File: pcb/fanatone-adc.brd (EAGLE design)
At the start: 49 x 32 mm, 43 parts, among them IC2 DIT4192-H, IC3 PCM4201-TSSOP-16, Q1 SST5484, U1 OPA1612AID, U2 TPS62240DRVTG4

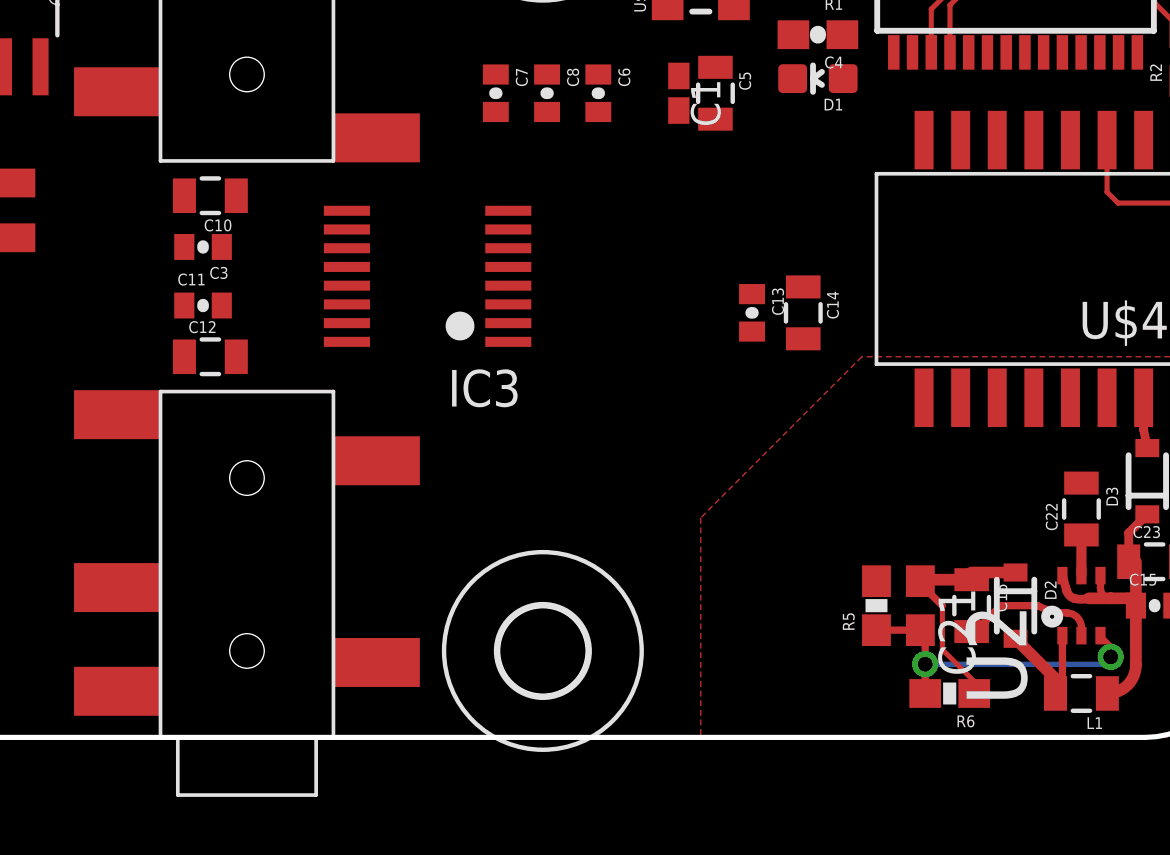
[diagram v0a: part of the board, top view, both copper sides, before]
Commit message: add datasheets, remove capacitor over R6 at booster
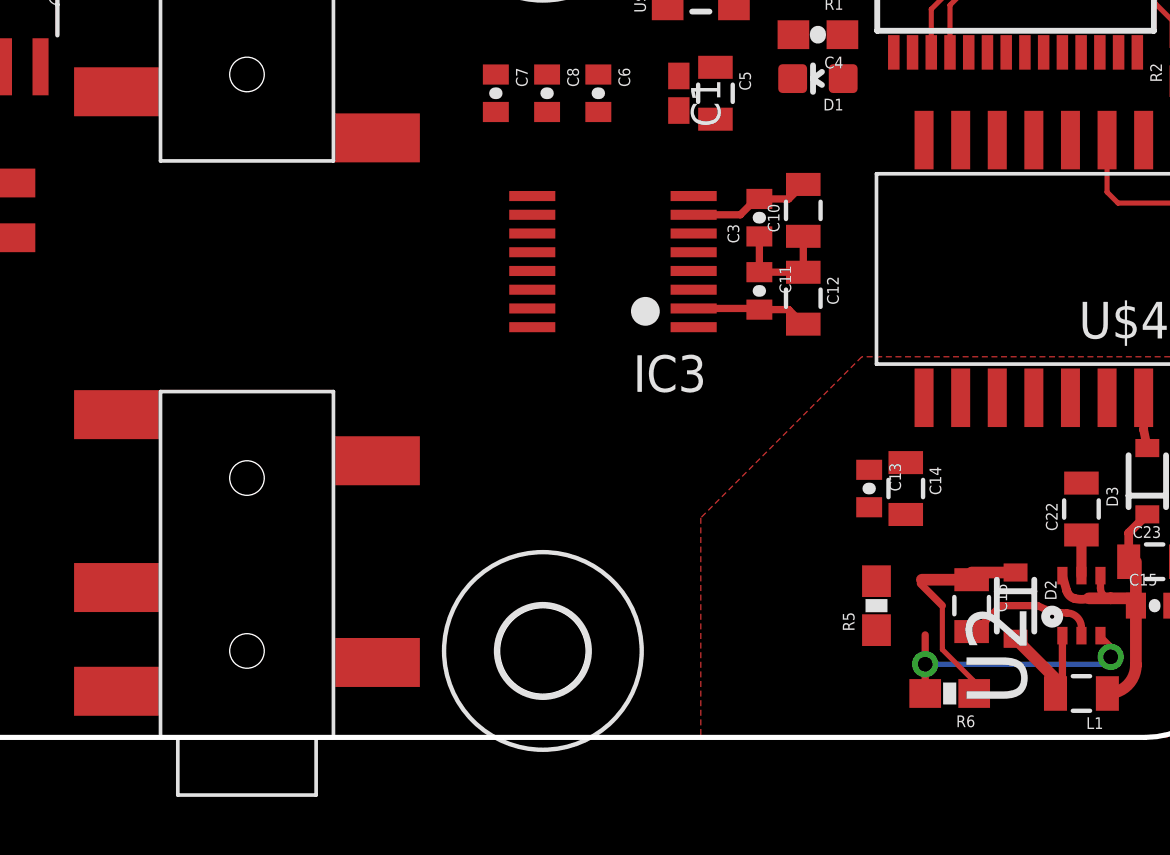
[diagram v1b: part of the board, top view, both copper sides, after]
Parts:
- removed C21: 4.7pF, rcl:C0603
- moved C12 20.7 mm to (34.0, 15.2), turned to 270 degrees
- moved C10 20.6 mm to (34.0, 18.3), turned to 90 degrees
- moved C3 19.3 mm to (32.5, 18.0), turned to 90 degrees
- moved C11 19.3 mm to (32.5, 15.5), turned to 270 degrees
- moved C13 7.33 mm to (36.3, 8.64)
- moved C14 7.06 mm to (37.6, 8.64)
- moved IC3 6.45 mm to (27.4, 16.5)
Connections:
- removed net 4V: C10.1, C3.1
- new net 5V: C11.2, C12.2, IC3.P$11
- new net N$12: IC2.11, IC3.P$2
- new net N$14: IC2.12, IC3.P$5
- new net N$15: IC2.13, IC3.P$3
- new net N$17: IC2.6, IC3.P$10
- net 3V3: now also IC3.P$12
- net GND: now also C10.1, C3.1, IC3.P$16, IC3.P$4, IC3.P$7, IC3.P$9; no longer C10.2, C3.2
- net N$5: now also C10.2, C3.2, IC3.P$15; no longer C11.2, C12.2
- net N$7: no longer C21.2
- net VCAPSULE: no longer C21.1
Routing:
- net N$5: track 0.00 -> 4.24 mm
- net 5V: track 0.00 -> 4.03 mm
- net GND: track 6.33 -> 10.3 mm
- net N$7: track 11.4 -> 9.64 mm

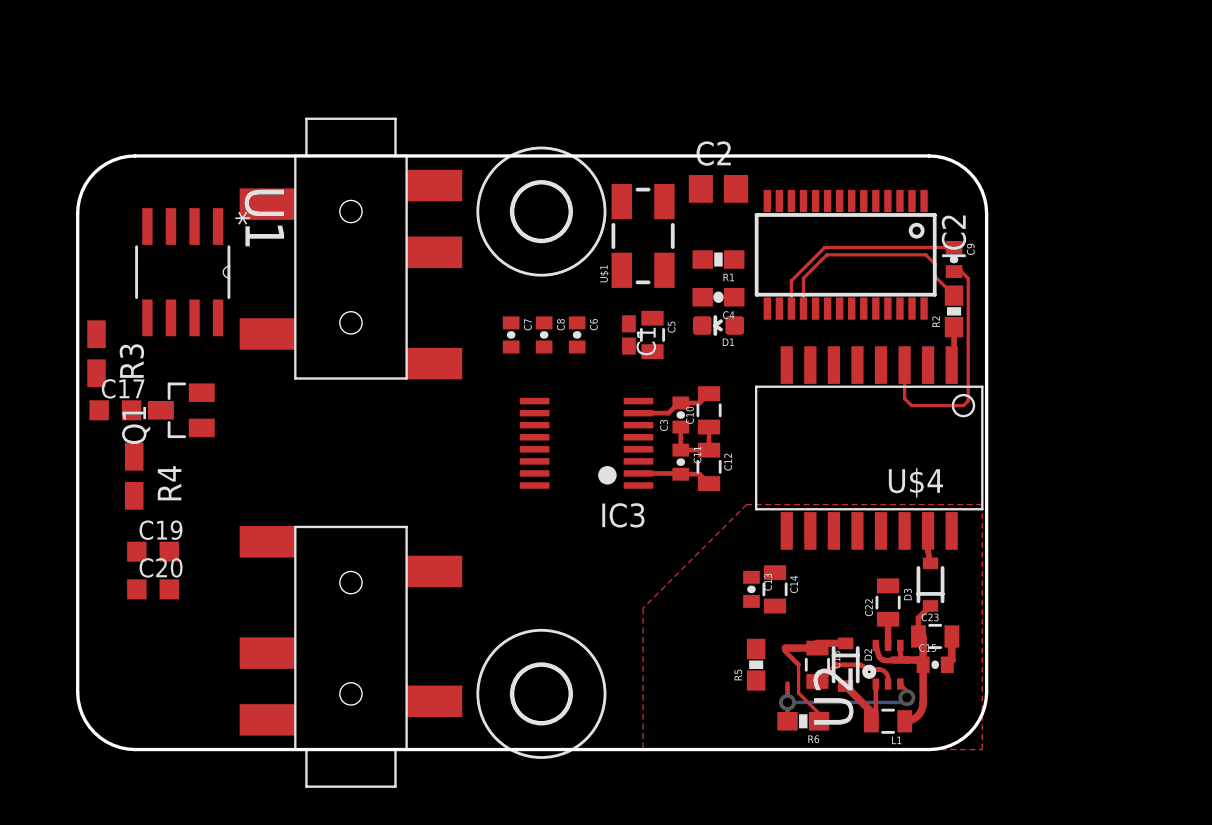
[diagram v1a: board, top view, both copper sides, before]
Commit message: Rectangular FAT Capsule R design
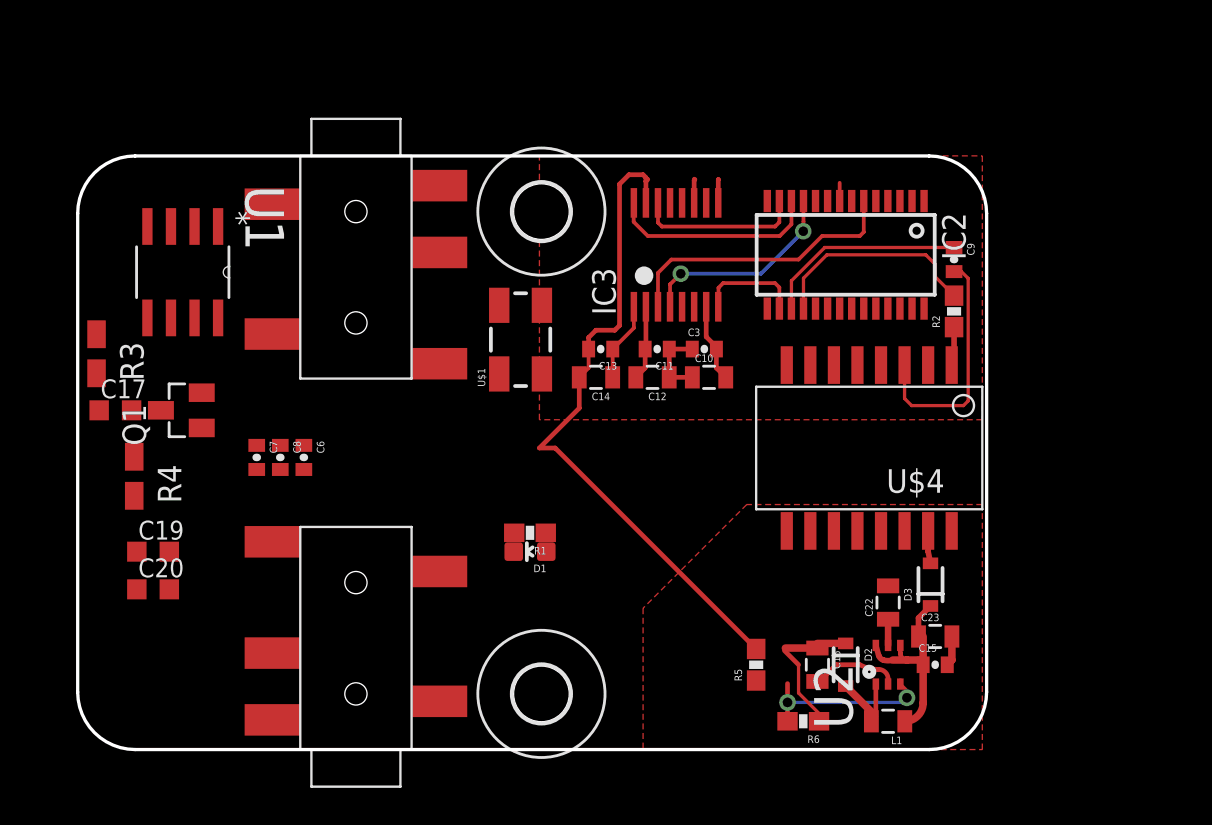
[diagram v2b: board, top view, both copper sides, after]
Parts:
- removed C1: (no value), rcl:C0402K
- removed C2: (no value), rcl:C0805
- removed C4: (no value), SparkFun-Passives:0603-CAP
- removed C5: (no value), SparkFun-Passives:0805
- moved R1 17.9 mm to (24.4, 11.7)
- moved C6 16.1 mm to (12.2, 15.7)
- moved D1 15.9 mm to (24.4, 10.7)
- moved C8 15.7 mm to (10.9, 15.7)
- moved C13 15.3 mm to (28.2, 21.6), turned to 180 degrees
- moved C7 15.2 mm to (9.65, 15.7)
- moved C14 15.0 mm to (27.9, 20.1), turned to 180 degrees
- moved IC3 11.2 mm to (32.3, 26.7), turned to 0 degrees
- moved U$1 8.65 mm to (23.9, 22.1)
- moved C11 6.23 mm to (31.2, 21.6), turned to 180 degrees
- moved C12 5.71 mm to (31.0, 20.1), turned to 180 degrees
- moved C3 3.78 mm to (33.8, 21.6), turned to 0 degrees
- moved C10 1.78 mm to (34.0, 20.1), turned to 0 degrees
- moved U$2 0.27 mm to (15.0, 32.0)
- moved U$3 0.27 mm to (15.0, 0.00)
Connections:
- new net N$19: IC3.P$13
- new net N$20: IC3.P$14
- net GND: now also IC3.P$6
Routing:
- net GND: track 10.3 -> 56.8 mm
- net N$17: track 0.00 -> 15.5 mm
- net N$14: track 0.00 -> 11.4 mm
- net N$12: track 0.00 -> 11.2 mm, vias 0 -> 2
- net N$15: track 0.00 -> 8.93 mm
- net 3V3: track 0.00 -> 4.28 mm

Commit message: start with OPA2134 at the initial gain stage
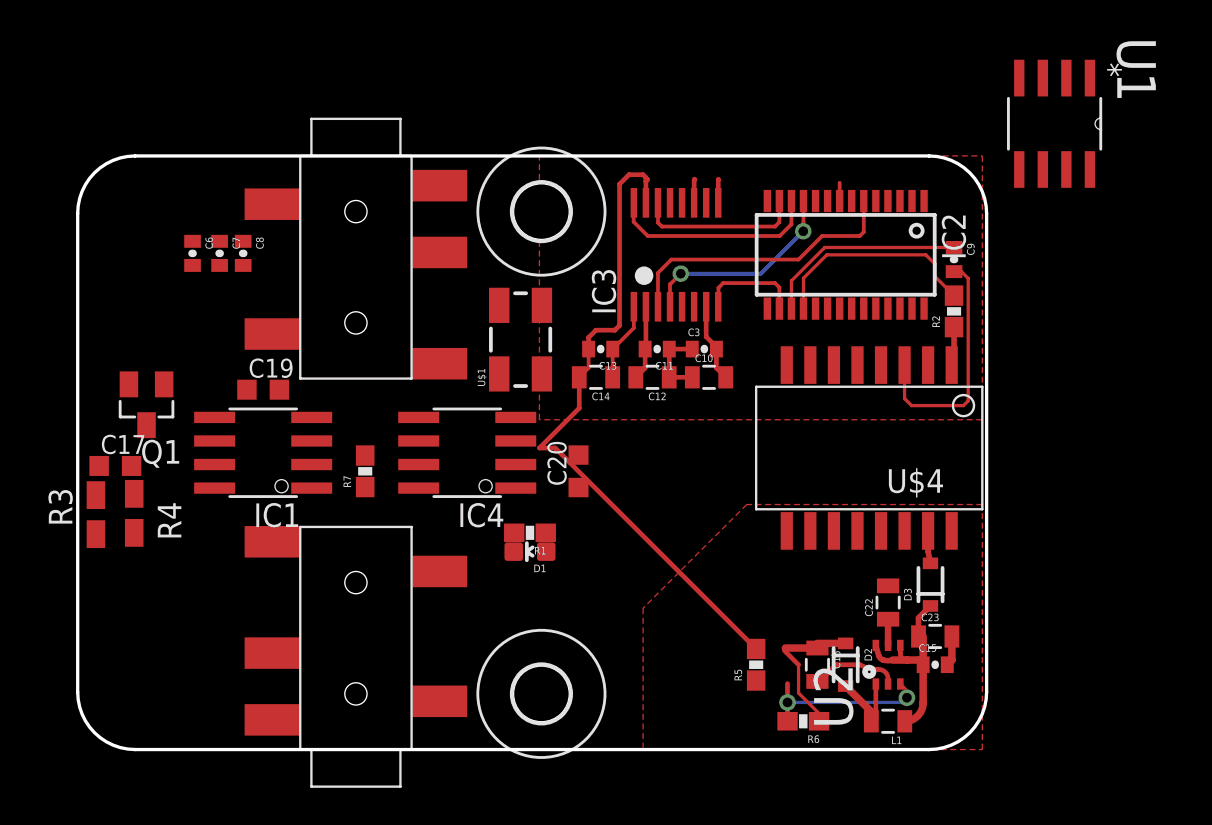
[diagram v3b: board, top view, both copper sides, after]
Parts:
- added IC1, IC4: OPA2134U, burr-brown:SO08
- added R7: (no value), SparkFun-Passives:0603-RES
- moved U1 47.7 mm to (52.7, 33.7)
- moved C20 23.8 mm to (27.0, 15.0), turned to 90 degrees
- moved C6 12.5 mm to (6.19, 26.7)
- moved C7 11.2 mm to (7.65, 26.7)
- moved C8 11.2 mm to (8.92, 26.7)
- moved C19 10.6 mm to (10.0, 19.4)
- moved R3 8.67 mm to (0.98, 12.7), turned to 90 degrees
- moved C17 3.00 mm to (2.03, 15.3)
- moved R4 2.00 mm to (3.05, 12.7)
- moved Q1 1.90 mm to (3.71, 18.6), turned to 180 degrees
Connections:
- new net N$21: IC1.1, R7.1
- new net N$22: IC1.2, R7.2
- new net N$23: IC1.4
- new net N$24: IC1.8
- new net N$25: IC4.8
- new net N$26: IC4.4
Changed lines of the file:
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@@
 <element name="C13" library="SparkFun-Passives" package="0402-CAP" value="100nF" x="28.194" y="21.59" rot="R180"/>
 <element name="C14" library="SparkFun-Passives" package="0805" value="10uF" x="27.94" y="20.066" rot="R180"/>
-<element name="C6" library="SparkFun-Passives" package="0402-CAP" value="100nF" x="12.192" y="15.748" rot="R270"/>
-<element name="C7" library="SparkFun-Passives" package="0402-CAP" value="100nF" x="9.652" y="15.748" rot="R270"/>
-<element name="C8" library="SparkFun-Passives" package="0402-CAP" value="100nF" x="10.922" y="15.748" rot="R270"/>
+<element name="C6" library="SparkFun-Passives" package="0402-CAP" value="100nF" x="6.192" y="26.748" rot="R270"/>
+<element name="C7" library="SparkFun-Passives" package="0402-CAP" value="100nF" x="7.652" y="26.748" rot="R270"/>
+<element name="C8" library="SparkFun-Passives" package="0402-CAP" value="100nF" x="8.922" y="26.748" rot="R270"/>
 <element name="C9" library="SparkFun-Passives" package="0402-CAP" value="100nF" x="47.244" y="26.416" rot="R270"/>
 <element name="D1" library="SparkFun-LED" package="LED-0603" value="BLUE" x="24.384" y="10.668" rot="R90">
@@
 <element name="U$2" library="PJ327A-TRS" package="PJ-327A" value="PJ-327A" x="15" y="32" rot="R270"/>
 <element name="U$3" library="PJ327A-TRS" package="PJ-327A" value="PJ-327A" x="15" y="0" rot="R90"/>
-<element name="Q1" library="transistor-fet" package="SOT23" value="SST5484" x="5.588" y="18.288" rot="R90"/>
-<element name="R3" library="rcl" package="R0805W" value="10M" x="1.016" y="21.336" rot="R270"/>
-<element name="C17" library="rcl" package="C0603K" value="" x="2.032" y="18.288"/>
-<element name="C19" library="rcl" package="C0603K" value="" x="4.064" y="10.668"/>
-<element name="C20" library="rcl" package="C0603K" value="" x="4.064" y="8.636"/>
-<element name="R4" library="rcl" package="R0805W" value="10M" x="3.048" y="14.732" rot="R270"/>
+<element name="Q1" library="transistor-fet" package="SOT23" value="SST5484" x="3.712" y="18.588" rot="R180"/>
+<element name="R3" library="rcl" package="R0805W" value="10M" x="0.984" y="12.664" rot="R90"/>
+<element name="C17" library="rcl" package="C0603K" value="" x="2.032" y="15.288"/>
+<element name="C19" library="rcl" package="C0603K" value="" x="10" y="19.4"/>
+<element name="C20" library="rcl" package="C0603K" value="" x="27" y="15" rot="R90"/>
+<element name="R4" library="rcl" package="R0805W" value="10M" x="3.048" y="12.732" rot="R270"/>
 <element name="D2" library="SparkFun-DiscreteSemi" package="SOD-323" value="PMEG4005EJ" x="41.402" y="4.572" rot="R270">
 <attribute name="PROD_ID" value="DIO-10955" x="41.402" y="4.572" size="1.778" layer="27" font="vector" ratio="15" rot="R270" display="off"/>
@@
 <attribute name="PROD_ID" value="DIO-10955" x="45.974" y="8.89" size="1.778" layer="27" font="vector" ratio="15" rot="R90" display="off"/>
 </element>
-<element name="U1" library="LT8330-boost-TSOT23" package="SOIC127P600X175-8N" value="OPA1612AID" x="5.664" y="25.734" rot="R270">
-<attribute name="OC_FARNELL" value="1754265" x="5.664" y="25.734" size="1.778" layer="27" font="vector" ratio="15" rot="R270" display="off"/>
-<attribute name="PACKAGE" value="SOIC-8" x="5.664" y="25.734" size="1.778" layer="27" font="vector" ratio="15" rot="R270" display="off"/>
-<attribute name="MPN" value="OPA1612AID" x="5.664" y="25.734" size="1.778" layer="27" font="vector" ratio="15" rot="R270" display="off"/>
-<attribute name="SUPPLIER" value="TI" x="5.664" y="25.734" size="1.778" layer="27" font="vector" ratio="15" rot="R270" display="off"/>
-<attribute name="OC_NEWARK" value="25R6133" x="5.664" y="25.734" size="1.778" layer="27" font="vector" ratio="15" rot="R270" display="off"/>
+<element name="U1" library="LT8330-boost-TSOT23" package="SOIC127P600X175-8N" value="OPA1612AID" x="52.664" y="33.734" rot="R270">
+<attribute name="OC_FARNELL" value="1754265" x="52.664" y="33.734" size="1.778" layer="27" font="vector" ratio="15" rot="R270" display="off"/>
+<attribute name="PACKAGE" value="SOIC-8" x="52.664" y="33.734" size="1.778" layer="27" font="vector" ratio="15" rot="R270" display="off"/>
+<attribute name="MPN" value="OPA1612AID" x="52.664" y="33.734" size="1.778" layer="27" font="vector" ratio="15" rot="R270" display="off"/>
+<attribute name="SUPPLIER" value="TI" x="52.664" y="33.734" size="1.778" layer="27" font="vector" ratio="15" rot="R270" display="off"/>
+<attribute name="OC_NEWARK" value="25R6133" x="52.664" y="33.734" size="1.778" layer="27" font="vector" ratio="15" rot="R270" display="off"/>
 </element>
 <element name="IC3" library="TI-PCM4201" package="TSSOP-16" value="PCM4201-TSSOP-16" x="32.258" y="26.67"/>
 <element name="C3" library="SparkFun-Passives" package="0402-CAP" value="100nF" x="33.782" y="21.59"/>
 <element name="C10" library="SparkFun-Passives" package="0805" value="10uF" x="34.036" y="20.066"/>
+<element name="IC1" library="burr-brown" package="SO08" value="OPA2134U" x="10" y="16" rot="R90">
+<attribute name="OC_FARNELL" value="1206935" x="10" y="16" size="1.778" layer="27" rot="R90" display="off"/>
+<attribute name="MPN" value="OPA2134UA" x="10" y="16" size="1.778" layer="27" rot="R90" display="off"/>
+<attribute name="MF" value="TEXAS INSTRUMENTS" x="10" y="16" size="1.778" layer="27" rot="R90" display="off"/>
+<attribute name="OC_NEWARK" value="35C1847" x="10" y="16" size="1.778" layer="27" rot="R90" display="off"/>
+</element>
+<element name="IC4" library="burr-brown" package="SO08" value="OPA2134U" x="21" y="16" rot="R90">
+<attribute name="OC_FARNELL" value="1206935" x="21" y="16" size="1.778" layer="27" rot="R90" display="off"/>
+<attribute name="MPN" value="OPA2134UA" x="21" y="16" size="1.778" layer="27" rot="R90" display="off"/>
+<attribute name="MF" value="TEXAS INSTRUMENTS" x="21" y="16" size="1.778" layer="27" rot="R90" display="off"/>
+<attribute name="OC_NEWARK" value="35C1847" x="21" y="16" size="1.778" layer="27" rot="R90" display="off"/>
+</element>
+<element name="R7" library="SparkFun-Passives" package="0603-RES" value="" x="15.5" y="15" rot="R90"/>
 </elements>
 <signals>
@@
 <contactref element="IC3" pad="P$6"/>
 <wire x1="29.21" y1="30.48" x2="19.5" y2="30.4" width="0" layer="19" extent="1-1"/>
-<wire x1="3.048" y1="13.6795" x2="24.892" y2="16.256" width="0" layer="19" extent="1-1"/>
+<wire x1="3.048" y1="11.6795" x2="24.892" y2="16.256" width="0" layer="19" extent="1-1"/>
 </signal>
 <signal name="3V3">
@@
 <contactref element="R3" pad="2"/>
 <contactref element="C17" pad="1"/>
-<wire x1="1.157" y1="18.288" x2="1.016" y2="20.2835" width="0" layer="19" extent="1-1"/>
+<wire x1="0.984" y1="13.7165" x2="1.157" y2="15.288" width="0" layer="19" extent="1-1"/>
 </signal>
 <signal name="N$4">
@@
 <contactref element="Q1" pad="3"/>
 <contactref element="R4" pad="1"/>
-<wire x1="4.488" y1="18.288" x2="2.907" y2="18.288" width="0" layer="19" extent="1-1"/>
-<wire x1="3.048" y1="15.7845" x2="2.907" y2="18.288" width="0" layer="19" extent="1-1"/>
+<wire x1="3.048" y1="13.7845" x2="2.907" y2="15.288" width="0" layer="19" extent="1-1"/>
+<wire x1="3.712" y1="17.488" x2="2.907" y2="15.288" width="0" layer="19" extent="1-1"/>
 </signal>
 <signal name="VCAPSULE">
@@
 <wire x1="39.966" y1="1.944" x2="39.966" y2="1.524" width="0.1778" layer="1"/>
 <wire x1="38.1" y1="5.334" x2="38.15" y2="5.472" width="0" layer="19" extent="1-1"/>
-<wire x1="1.016" y1="22.3885" x2="38.15" y2="5.472" width="0" layer="19" extent="1-1"/>
+<wire x1="0.984" y1="11.6115" x2="38.1" y2="5.334" width="0" layer="19" extent="1-1"/>
 </signal>
 <signal name="N$7">
@@
 <contactref element="IC3" pad="P$14"/>
 </signal>
+<signal name="N$21">
+<contactref element="R7" pad="1"/>
+<contactref element="IC1" pad="1"/>
+<wire x1="12.6162" y1="14.095" x2="15.5" y2="14.15" width="0" layer="19" extent="1-1"/>
+</signal>
+<signal name="N$22">
+<contactref element="IC1" pad="2"/>
+<contactref element="R7" pad="2"/>
+<wire x1="12.6162" y1="15.365" x2="15.5" y2="15.85" width="0" layer="19" extent="1-1"/>
+</signal>
+<signal name="N$23">
+<contactref element="IC1" pad="4"/>
+</signal>
+<signal name="N$24">
+<contactref element="IC1" pad="8"/>
+</signal>
+<signal name="N$25">
+<contactref element="IC4" pad="8"/>
+</signal>
+<signal name="N$26">
+<contactref element="IC4" pad="4"/>
+</signal>
 </signals>
